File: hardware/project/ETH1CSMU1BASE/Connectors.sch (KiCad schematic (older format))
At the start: 5 parts

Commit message: Schematic developement, new footprints.
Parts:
- J504: renamed from J?; footprint (none) -> ETH1CSMU1:Socket_DIN41612-CaseC1-AC-Male-64Pin-2rows
- gave numbers to parts that had none: 4
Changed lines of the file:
@@
 $Descr A4 11693 8268
 encoding utf-8
-Sheet 5 6
+Sheet 5 7
 Title ""
 Date ""
@@
 $EndDescr
 $Comp
-L Connector:C64AC J?
+L Connector:C64AC J504
 U 1 1 5DE8758D
 P 5550 4150
-F 0 "J?" H 5730 4246 50  0000 L CNN
+F 0 "J504" H 5730 4246 50  0000 L CNN
 F 1 "C64AC" H 5730 4155 50  0000 L CNN
-F 2 "" H 5550 4200 50  0001 C CNN
+F 2 "ETH1CSMU1:Socket_DIN41612-CaseC1-AC-Male-64Pin-2rows" H 5550 4200 50  0001 C CNN
 F 3 " ~" H 5550 4200 50  0001 C CNN
 	1    5550 4150
@@
 	5200 7150 5200 7100
 $Comp
-L power:+24V #PWR?
+L power:+24V #PWR0116
 U 1 1 5DE97137
 P 5150 7100
-F 0 "#PWR?" H 5150 6950 50  0001 C CNN
+F 0 "#PWR0116" H 5150 6950 50  0001 C CNN
 F 1 "+24V" V 5165 7228 50  0000 L CNN
 F 2 "" H 5150 7100 50  0001 C CNN
@@
 	5200 6350 5200 6300
 $Comp
-L power:GND #PWR?
+L power:GND #PWR0117
 U 1 1 5DE992F4
 P 5150 6300
-F 0 "#PWR?" H 5150 6050 50  0001 C CNN
+F 0 "#PWR0117" H 5150 6050 50  0001 C CNN
 F 1 "GND" V 5155 6172 50  0000 R CNN
 F 2 "" H 5150 6300 50  0001 C CNN
@@
 F
 $Comp
-L Connector_Generic:Conn_01x06 J?
+L Connector_Generic:Conn_01x06 J501
 U 1 1 5DEBCC80
 P 2750 2400
-F 0 "J?" H 2668 2817 50  0000 C CNN
+F 0 "J501" H 2668 2817 50  0000 C CNN
 F 1 "Conn_01x06" H 2668 2726 50  0000 C CNN
 F 2 "" H 2750 2400 50  0001 C CNN
@@
 	5200 5250 5250 5250
 $Comp
-L power:Earth #PWR?
+L power:Earth #PWR0118
 U 1 1 5DECE77F
 P 5150 5200
-F 0 "#PWR?" H 5150 4950 50  0001 C CNN
+F 0 "#PWR0118" H 5150 4950 50  0001 C CNN
 F 1 "Earth" H 5150 5050 50  0001 C CNN
 F 2 "" H 5150 5200 50  0001 C CNN
@@
 	5200 4450 5250 4450
 $Comp
-L power:Earth #PWR?
+L power:Earth #PWR0119
 U 1 1 5DED2C4C
 P 5150 4400
-F 0 "#PWR?" H 5150 4150 50  0001 C CNN
+F 0 "#PWR0119" H 5150 4150 50  0001 C CNN
 F 1 "Earth" H 5150 4250 50  0001 C CNN
 F 2 "" H 5150 4400 50  0001 C CNN
@@
 TX-
 $Comp
-L ETH1CSMU1:GND_TRIG #PWR?
+L ETH1CSMU1:GND_TRIG #PWR0120
 U 1 1 5EC065BC
 P 5200 4050
-F 0 "#PWR?" H 5200 3800 50  0001 C CNN
+F 0 "#PWR0120" H 5200 3800 50  0001 C CNN
 F 1 "GND_TRIG" V 5205 3922 50  0000 R CNN
 F 2 "" H 5200 4050 50  0001 C CNN
@@
 	5200 3950 5250 3950
 $Comp
-L ETH1CSMU1:ADuM3151 U?
+L ETH1CSMU1:ADuM3151 U501
 U 1 1 5DCFA591
 P 8050 1800
-F 0 "U?" H 8050 2665 50  0000 C CNN
+F 0 "U501" H 8050 2665 50  0000 C CNN
 F 1 "ADuM3151" H 8050 2574 50  0000 C CNN
 F 2 "" H 9950 2250 50  0001 C CNN
@@
 BASE_~MSS
 $Comp
-L power:+3.3V #PWR?
+L power:+3.3V #PWR0121
 U 1 1 5DCFA59E
 P 7250 1100
-F 0 "#PWR?" H 7250 950 50  0001 C CNN
+F 0 "#PWR0121" H 7250 950 50  0001 C CNN
 F 1 "+3.3V" H 7265 1273 50  0000 C CNN
 F 2 "" H 7250 1100 50  0001 C CNN
@@
 	7250 2400 7350 2400
 $Comp
-L power:GND #PWR?
+L power:GND #PWR0122
 U 1 1 5DCFA5A9
 P 7250 2500
-F 0 "#PWR?" H 7250 2250 50  0001 C CNN
+F 0 "#PWR0122" H 7250 2250 50  0001 C CNN
 F 1 "GND" H 7255 2327 50  0000 C CNN
 F 2 "" H 7250 2500 50  0001 C CNN
@@
 Connection ~ 7250 2400
 $Comp
-L power:+3.3VP #PWR?
+L power:+3.3VP #PWR0123
 U 1 1 5DD4087A
 P 8850 1100
-F 0 "#PWR?" H 9000 1050 50  0001 C CNN
+F 0 "#PWR0123" H 9000 1050 50  0001 C CNN
 F 1 "+3.3VP" H 8870 1243 50  0000 C CNN
 F 2 "" H 8850 1100 50  0001 C CNN
@@
 Connection ~ 8850 2400
 $Comp
-L ETH1CSMU1:GNDS #PWR?
+L ETH1CSMU1:GNDS #PWR0124
 U 1 1 5DD73568
 P 8850 2500
-F 0 "#PWR?" H 8850 2250 50  0001 C CNN
+F 0 "#PWR0124" H 8850 2250 50  0001 C CNN
 F 1 "GNDS" H 8855 2327 50  0000 C CNN
 F 2 "" H 8850 2500 50  0001 C CNN
@@
 	7300 1900 7350 1900
 $Comp
-L Connector_Generic:Conn_02x10_Odd_Even J?
+L Connector_Generic:Conn_02x10_Odd_Even J502
 U 1 1 5DD815E6
 P 8000 3600
-F 0 "J?" H 8050 4217 50  0000 C CNN
+F 0 "J502" H 8050 4217 50  0000 C CNN
 F 1 "Conn_02x10_Odd_Even" H 8050 4126 50  0000 C CNN
 F 2 "" H 8000 3600 50  0001 C CNN
@@
 MODULE_~MSS
 $Comp
-L ETH1CSMU1:GNDS #PWR?
+L ETH1CSMU1:GNDS #PWR0125
 U 1 1 5DE4A93E
 P 7700 4100
-F 0 "#PWR?" H 7700 3850 50  0001 C CNN
+F 0 "#PWR0125" H 7700 3850 50  0001 C CNN
 F 1 "GNDS" V 7705 3972 50  0000 R CNN
 F 2 "" H 7700 4100 50  0001 C CNN
@@
 	7000 3500 7800 3500
 $Comp
-L power:+3.3VP #PWR?
+L power:+3.3VP #PWR0126
 U 1 1 5DE5F329
 P 7750 3200
-F 0 "#PWR?" H 7900 3150 50  0001 C CNN
+F 0 "#PWR0126" H 7900 3150 50  0001 C CNN
 F 1 "+3.3VP" V 7750 3300 50  0000 L CNN
 F 2 "" H 7750 3200 50  0001 C CNN
@@
 	8300 3300 9100 3300
 $Comp
-L power:+3.3VP #PWR?
+L power:+3.3VP #PWR0127
 U 1 1 5DE90B41
 P 8350 3200
-F 0 "#PWR?" H 8500 3150 50  0001 C CNN
+F 0 "#PWR0127" H 8500 3150 50  0001 C CNN
 F 1 "+3.3VP" V 8350 3300 50  0000 L CNN
 F 2 "" H 8350 3200 50  0001 C CNN
@@
 	7750 4100 7800 4100
 $Comp
-L ETH1CSMU1:GNDS #PWR?
+L ETH1CSMU1:GNDS #PWR0128
 U 1 1 5DEB2514
 P 8400 4100
-F 0 "#PWR?" H 8400 3850 50  0001 C CNN
+F 0 "#PWR0128" H 8400 3850 50  0001 C CNN
 F 1 "GNDS" V 8405 3972 50  0000 R CNN
 F 2 "" H 8400 4100 50  0001 C CNN
@@
 	8350 4100 8300 4100
 $Comp
-L ETH1CSMU1:+HV #PWR?
+L ETH1CSMU1:+HV #PWR0129
 U 1 1 5DECC2A8
 P 2400 3500
-F 0 "#PWR?" H 2400 3350 50  0001 C CNN
+F 0 "#PWR0129" H 2400 3350 50  0001 C CNN
 F 1 "+HV" V 2400 3650 50  0000 L CNN
 F 2 "" H 2400 3500 50  0001 C CNN
@@
 	2400 3500 2500 3500
 $Comp
-L ETH1CSMU1:+HV #PWR?
+L ETH1CSMU1:+HV #PWR0130
 U 1 1 5DED1199
 P 3100 3500
-F 0 "#PWR?" H 3100 3350 50  0001 C CNN
+F 0 "#PWR0130" H 3100 3350 50  0001 C CNN
 F 1 "+HV" V 3100 3650 50  0000 L CNN
 F 2 "" H 3100 3500 50  0001 C CNN
@@
 NoConn ~ 3000 3600
 $Comp
-L ETH1CSMU1:-HV #PWR?
+L ETH1CSMU1:-HV #PWR0131
 U 1 1 5DEDEAA7
 P 2400 3700
-F 0 "#PWR?" H 2400 3550 50  0001 C CNN
+F 0 "#PWR0131" H 2400 3550 50  0001 C CNN
 F 1 "-HV" V 2400 3850 50  0000 L CNN
 F 2 "" H 2400 3700 50  0001 C CNN
@@
 	2400 3700 2500 3700
 $Comp
-L ETH1CSMU1:-HV #PWR?
+L ETH1CSMU1:-HV #PWR0132
 U 1 1 5DEE33FC
 P 3100 3700
-F 0 "#PWR?" H 3100 3550 50  0001 C CNN
+F 0 "#PWR0132" H 3100 3550 50  0001 C CNN
 F 1 "-HV" V 3100 3850 50  0000 L CNN
 F 2 "" H 3100 3700 50  0001 C CNN
@@
 	3100 3700 3000 3700
 $Comp
-L ETH1CSMU1:GNDHV #PWR?
+L ETH1CSMU1:GNDHV #PWR0133
 U 1 1 5DF1922C
 P 2400 3950
-F 0 "#PWR?" H 2400 3700 50  0001 C CNN
+F 0 "#PWR0133" H 2400 3700 50  0001 C CNN
 F 1 "GNDHV" V 2405 3822 50  0000 R CNN
 F 2 "" H 2400 3950 50  0001 C CNN
@@
 	2450 3950 2450 4000
 $Comp
-L ETH1CSMU1:GNDHV #PWR?
+L ETH1CSMU1:GNDHV #PWR0134
 U 1 1 5DF55BC0
 P 3100 3950
-F 0 "#PWR?" H 3100 3700 50  0001 C CNN
+F 0 "#PWR0134" H 3100 3700 50  0001 C CNN
 F 1 "GNDHV" V 3105 3822 50  0000 R CNN
 F 2 "" H 3100 3950 50  0001 C CNN
@@
 NoConn ~ 3000 4100
 $Comp
-L power:+5VL #PWR?
+L power:+5VL #PWR0135
 U 1 1 5DF6C00E
 P 2400 4400
-F 0 "#PWR?" H 2400 4250 50  0001 C CNN
+F 0 "#PWR0135" H 2400 4250 50  0001 C CNN
 F 1 "+5VL" V 2415 4527 50  0000 L CNN
 F 2 "" H 2400 4400 50  0001 C CNN
@@
 	2400 4400 2500 4400
 $Comp
-L power:+5VL #PWR?
+L power:+5VL #PWR0136
 U 1 1 5DF71C9F
 P 3100 4400
-F 0 "#PWR?" H 3100 4250 50  0001 C CNN
+F 0 "#PWR0136" H 3100 4250 50  0001 C CNN
 F 1 "+5VL" V 3115 4528 50  0000 L CNN
 F 2 "" H 3100 4400 50  0001 C CNN
@@
 	3100 4400 3000 4400
 $Comp
-L power:+3.3VP #PWR?
+L power:+3.3VP #PWR0137
 U 1 1 5DF78ED7
 P 2400 4500
-F 0 "#PWR?" H 2550 4450 50  0001 C CNN
+F 0 "#PWR0137" H 2550 4450 50  0001 C CNN
 F 1 "+3.3VP" V 2400 4600 50  0000 L CNN
 F 2 "" H 2400 4500 50  0001 C CNN
@@
 	2400 4500 2500 4500
 $Comp
-L power:+3.3VP #PWR?
+L power:+3.3VP #PWR0138
 U 1 1 5DF7F2B1
 P 3100 4500
-F 0 "#PWR?" H 3250 4450 50  0001 C CNN
+F 0 "#PWR0138" H 3250 4450 50  0001 C CNN
 F 1 "+3.3VP" V 3100 4600 50  0000 L CNN
 F 2 "" H 3100 4500 50  0001 C CNN
@@
 	3100 4500 3000 4500
 $Comp
-L power:+15V #PWR?
+L power:+15V #PWR0139
 U 1 1 5DF9592E
 P 2400 4200
-F 0 "#PWR?" H 2400 4050 50  0001 C CNN
+F 0 "#PWR0139" H 2400 4050 50  0001 C CNN
 F 1 "+15V" V 2400 4350 50  0000 L CNN
 F 2 "" H 2400 4200 50  0001 C CNN
@@
 	2400 4200 2500 4200
 $Comp
-L power:+15V #PWR?
+L power:+15V #PWR0140
 U 1 1 5DF9D7C3
 P 3100 4200
-F 0 "#PWR?" H 3100 4050 50  0001 C CNN
+F 0 "#PWR0140" H 3100 4050 50  0001 C CNN
 F 1 "+15V" V 3100 4350 50  0000 L CNN
 F 2 "" H 3100 4200 50  0001 C CNN
@@
 	3100 4200 3000 4200
 $Comp
-L power:-15V #PWR?
+L power:-15V #PWR0141
 U 1 1 5DFBFA3C
 P 2400 4300
-F 0 "#PWR?" H 2400 4400 50  0001 C CNN
+F 0 "#PWR0141" H 2400 4400 50  0001 C CNN
 F 1 "-15V" V 2400 4450 50  0000 L CNN
 F 2 "" H 2400 4300 50  0001 C CNN
@@
 	2400 4300 2500 4300
 $Comp
-L power:-15V #PWR?
+L power:-15V #PWR0142
 U 1 1 5DFCED5E
 P 3100 4300
-F 0 "#PWR?" H 3100 4400 50  0001 C CNN
+F 0 "#PWR0142" H 3100 4400 50  0001 C CNN
 F 1 "-15V" V 3100 4450 50  0000 L CNN
 F 2 "" H 3100 4300 50  0001 C CNN
@@
 	3100 4300 3000 4300
 $Comp
-L Connector_Generic:Conn_02x14_Odd_Even J?
+L Connector_Generic:Conn_02x14_Odd_Even J503
 U 1 1 5DFFC045
 P 2700 4100
-F 0 "J?" H 2750 4917 50  0000 C CNN
+F 0 "J503" H 2750 4917 50  0000 C CNN
 F 1 "Conn_02x14_Odd_Even" H 2750 4826 50  0000 C CNN
 F 2 "" H 2700 4100 50  0001 C CNN
@@
 	3050 4800 3000 4800
 $Comp
-L ETH1CSMU1:GNDS #PWR?
+L ETH1CSMU1:GNDS #PWR0143
 U 1 1 5E00D610
 P 2400 4750
-F 0 "#PWR?" H 2400 4500 50  0001 C CNN
+F 0 "#PWR0143" H 2400 4500 50  0001 C CNN
 F 1 "GNDS" V 2400 4600 50  0000 R CNN
 F 2 "" H 2400 4750 50  0001 C CNN
@@
 	2450 4750 2450 4800
 $Comp
-L ETH1CSMU1:GNDS #PWR?
+L ETH1CSMU1:GNDS #PWR0144
 U 1 1 5E015B37
 P 3100 4750
-F 0 "#PWR?" H 3100 4500 50  0001 C CNN
+F 0 "#PWR0144" H 3100 4500 50  0001 C CNN
 F 1 "GNDS" V 3100 4600 50  0000 R CNN
 F 2 "" H 3100 4750 50  0001 C CNN

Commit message: Schematic design.
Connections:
- net labels removed: +15V, +5VL, +HV, -15V, -HV, GNDHV
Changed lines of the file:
@@
 $Descr A4 11693 8268
 encoding utf-8
-Sheet 5 7
+Sheet 5 9
 Title ""
 Date ""
@@
 Wire Wire Line
 	8350 4100 8300 4100
-$Comp
-L ETH1CSMU1:+HV #PWR0129
-U 1 1 5DECC2A8
-P 2400 3500
-F 0 "#PWR0129" H 2400 3350 50  0001 C CNN
-F 1 "+HV" V 2400 3650 50  0000 L CNN
-F 2 "" H 2400 3500 50  0001 C CNN
-F 3 "" H 2400 3500 50  0001 C CNN
-	1    2400 3500
-	0    -1   -1   0
-$EndComp
 Wire Wire Line
 	2400 3500 2500 3500
-$Comp
-L ETH1CSMU1:+HV #PWR0130
-U 1 1 5DED1199
-P 3100 3500
-F 0 "#PWR0130" H 3100 3350 50  0001 C CNN
-F 1 "+HV" V 3100 3650 50  0000 L CNN
-F 2 "" H 3100 3500 50  0001 C CNN
-F 3 "" H 3100 3500 50  0001 C CNN
-	1    3100 3500
-	0    1    1    0
-$EndComp
 Wire Wire Line
 	3100 3500 3000 3500
 NoConn ~ 2500 3600
 NoConn ~ 3000 3600
-$Comp
-L ETH1CSMU1:-HV #PWR0131
-U 1 1 5DEDEAA7
-P 2400 3700
-F 0 "#PWR0131" H 2400 3550 50  0001 C CNN
-F 1 "-HV" V 2400 3850 50  0000 L CNN
-F 2 "" H 2400 3700 50  0001 C CNN
-F 3 "" H 2400 3700 50  0001 C CNN
-	1    2400 3700
-	0    -1   -1   0
-$EndComp
 Wire Wire Line
 	2400 3700 2500 3700
-$Comp
-L ETH1CSMU1:-HV #PWR0132
-U 1 1 5DEE33FC
-P 3100 3700
-F 0 "#PWR0132" H 3100 3550 50  0001 C CNN
-F 1 "-HV" V 3100 3850 50  0000 L CNN
-F 2 "" H 3100 3700 50  0001 C CNN
-F 3 "" H 3100 3700 50  0001 C CNN
-	1    3100 3700
-	0    1    1    0
-$EndComp
 Wire Wire Line
 	3100 3700 3000 3700
-$Comp
-L ETH1CSMU1:GNDHV #PWR0133
-U 1 1 5DF1922C
-P 2400 3950
-F 0 "#PWR0133" H 2400 3700 50  0001 C CNN
-F 1 "GNDHV" V 2405 3822 50  0000 R CNN
-F 2 "" H 2400 3950 50  0001 C CNN
-F 3 "" H 2400 3950 50  0001 C CNN
-	1    2400 3950
-	0    1    1    0
-$EndComp
 NoConn ~ 2500 3800
 NoConn ~ 3000 3800
@@
 Wire Wire Line
 	2450 3950 2450 4000
-$Comp
-L ETH1CSMU1:GNDHV #PWR0134
-U 1 1 5DF55BC0
-P 3100 3950
-F 0 "#PWR0134" H 3100 3700 50  0001 C CNN
-F 1 "GNDHV" V 3105 3822 50  0000 R CNN
-F 2 "" H 3100 3950 50  0001 C CNN
-F 3 "" H 3100 3950 50  0001 C CNN
-	1    3100 3950
-	0    -1   -1   0
-$EndComp
 Wire Wire Line
 	3000 4000 3050 4000
@@
 NoConn ~ 2500 4100
 NoConn ~ 3000 4100
-$Comp
-L power:+5VL #PWR0135
-U 1 1 5DF6C00E
-P 2400 4400
-F 0 "#PWR0135" H 2400 4250 50  0001 C CNN
-F 1 "+5VL" V 2415 4527 50  0000 L CNN
-F 2 "" H 2400 4400 50  0001 C CNN
-F 3 "" H 2400 4400 50  0001 C CNN
-	1    2400 4400
-	0    -1   -1   0
-$EndComp
 Wire Wire Line
 	2400 4400 2500 4400
-$Comp
-L power:+5VL #PWR0136
-U 1 1 5DF71C9F
-P 3100 4400
-F 0 "#PWR0136" H 3100 4250 50  0001 C CNN
-F 1 "+5VL" V 3115 4528 50  0000 L CNN
-F 2 "" H 3100 4400 50  0001 C CNN
-F 3 "" H 3100 4400 50  0001 C CNN
-	1    3100 4400
-	0    1    1    0
-$EndComp
 Wire Wire Line
 	3100 4400 3000 4400
-$Comp
-L power:+3.3VP #PWR0137
-U 1 1 5DF78ED7
-P 2400 4500
-F 0 "#PWR0137" H 2550 4450 50  0001 C CNN
-F 1 "+3.3VP" V 2400 4600 50  0000 L CNN
-F 2 "" H 2400 4500 50  0001 C CNN
-F 3 "" H 2400 4500 50  0001 C CNN
-	1    2400 4500
-	0    -1   -1   0
-$EndComp
 Wire Wire Line
 	2400 4500 2500 4500
-$Comp
-L power:+3.3VP #PWR0138
-U 1 1 5DF7F2B1
-P 3100 4500
-F 0 "#PWR0138" H 3250 4450 50  0001 C CNN
-F 1 "+3.3VP" V 3100 4600 50  0000 L CNN
-F 2 "" H 3100 4500 50  0001 C CNN
-F 3 "" H 3100 4500 50  0001 C CNN
-	1    3100 4500
-	0    1    1    0
-$EndComp
 Wire Wire Line
 	3100 4500 3000 4500
-$Comp
-L power:+15V #PWR0139
-U 1 1 5DF9592E
-P 2400 4200
-F 0 "#PWR0139" H 2400 4050 50  0001 C CNN
-F 1 "+15V" V 2400 4350 50  0000 L CNN
-F 2 "" H 2400 4200 50  0001 C CNN
-F 3 "" H 2400 4200 50  0001 C CNN
-	1    2400 4200
-	0    -1   -1   0
-$EndComp
 Wire Wire Line
 	2400 4200 2500 4200
-$Comp
-L power:+15V #PWR0140
-U 1 1 5DF9D7C3
-P 3100 4200
-F 0 "#PWR0140" H 3100 4050 50  0001 C CNN
-F 1 "+15V" V 3100 4350 50  0000 L CNN
-F 2 "" H 3100 4200 50  0001 C CNN
-F 3 "" H 3100 4200 50  0001 C CNN
-	1    3100 4200
-	0    1    1    0
-$EndComp
 Wire Wire Line
 	3100 4200 3000 4200
-$Comp
-L power:-15V #PWR0141
-U 1 1 5DFBFA3C
-P 2400 4300
-F 0 "#PWR0141" H 2400 4400 50  0001 C CNN
-F 1 "-15V" V 2400 4450 50  0000 L CNN
-F 2 "" H 2400 4300 50  0001 C CNN
-F 3 "" H 2400 4300 50  0001 C CNN
-	1    2400 4300
-	0    -1   -1   0
-$EndComp
 Wire Wire Line
 	2400 4300 2500 4300
-$Comp
-L power:-15V #PWR0142
-U 1 1 5DFCED5E
-P 3100 4300
-F 0 "#PWR0142" H 3100 4400 50  0001 C CNN
-F 1 "-15V" V 3100 4450 50  0000 L CNN
-F 2 "" H 3100 4300 50  0001 C CNN
-F 3 "" H 3100 4300 50  0001 C CNN
-	1    3100 4300
-	0    1    1    0
-$EndComp
 Wire Wire Line
 	3100 4300 3000 4300
@@
 Wire Wire Line
 	3050 4800 3000 4800
-$Comp
-L ETH1CSMU1:GNDS #PWR0143
-U 1 1 5E00D610
-P 2400 4750
-F 0 "#PWR0143" H 2400 4500 50  0001 C CNN
-F 1 "GNDS" V 2400 4600 50  0000 R CNN
-F 2 "" H 2400 4750 50  0001 C CNN
-F 3 "" H 2400 4750 50  0001 C CNN
-	1    2400 4750
-	0    1    1    0
-$EndComp
 Wire Wire Line
 	2400 4750 2450 4750
@@
 Wire Wire Line
 	2450 4750 2450 4800
-$Comp
-L ETH1CSMU1:GNDS #PWR0144
-U 1 1 5E015B37
-P 3100 4750
-F 0 "#PWR0144" H 3100 4500 50  0001 C CNN
-F 1 "GNDS" V 3100 4600 50  0000 R CNN
-F 2 "" H 3100 4750 50  0001 C CNN
-F 3 "" H 3100 4750 50  0001 C CNN
-	1    3100 4750
-	0    -1   -1   0
-$EndComp
 Wire Wire Line
 	3100 4750 3050 4750

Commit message: Power supply design
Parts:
- removed J502: Conn_02x10_Odd_Even, symbol Connector_Generic:Conn_02x10_Odd_Even
- removed J503: Conn_02x14_Odd_Even, symbol Connector_Generic:Conn_02x14_Odd_Even
- added J?: Conn_02x08_Odd_Even, symbol Connector_Generic:Conn_02x08_Odd_Even
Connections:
- net labels added: +3.3VF, GNDF
- net labels removed: +3.3VP, GNDS
- wire segments 152 -> 112
- no-connect marks 32 -> 26
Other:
- moved on the sheet: J501, U501

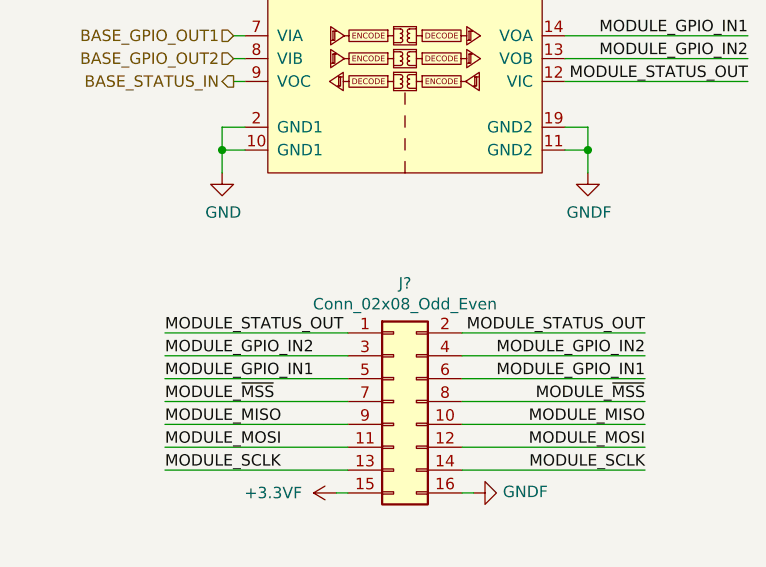
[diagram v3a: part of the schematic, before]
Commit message: Footprint assigment
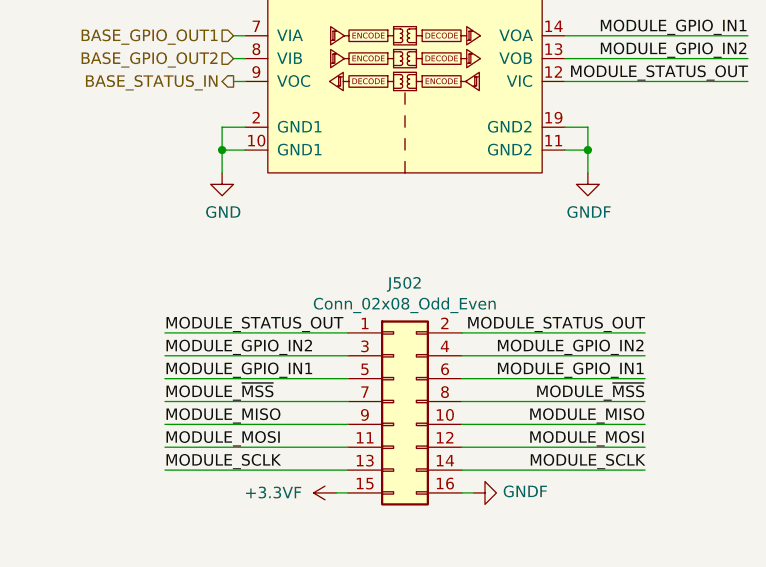
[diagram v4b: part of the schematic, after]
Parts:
- U501: footprint (none) -> Package_SO:SSOP-20_5.3x7.2mm_P0.65mm
- gave numbers to parts that had none: 1
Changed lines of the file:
@@
 F 0 "U501" H 9000 2515 50  0000 C CNN
 F 1 "ADuM3151" H 9000 2424 50  0000 C CNN
-F 2 "" H 10900 2100 50  0001 C CNN
+F 2 "Package_SO:SSOP-20_5.3x7.2mm_P0.65mm" H 10900 2100 50  0001 C CNN
 F 3 "" H 10900 2100 50  0001 C CNN
 	1    9000 1650
@@
 MODULE_GPIO_IN1
 $Comp
-L ETH1CSMU1:+3.3VF #PWR?
+L ETH1CSMU1:+3.3VF #PWR0108
 U 1 1 6828C08F
 P 9800 950
-F 0 "#PWR?" H 9800 800 50  0001 C CNN
+F 0 "#PWR0108" H 9800 800 50  0001 C CNN
 F 1 "+3.3VF" H 9815 1123 50  0000 C CNN
 F 2 "" H 9800 950 50  0001 C CNN
@@
 $EndComp
 $Comp
-L ETH1CSMU1:GNDF #PWR?
+L ETH1CSMU1:GNDF #PWR0123
 U 1 1 6828CBFD
 P 9800 2350
-F 0 "#PWR?" H 9800 2100 50  0001 C CNN
+F 0 "#PWR0123" H 9800 2100 50  0001 C CNN
 F 1 "GNDF" H 9805 2177 50  0000 C CNN
 F 2 "" H 9800 2350 50  0001 C CNN
@@
 $EndComp
 $Comp
-L ETH1CSMU1:+3.3VF #PWR?
+L ETH1CSMU1:+3.3VF #PWR0124
 U 1 1 6829671C
 P 8700 3750
-F 0 "#PWR?" H 8700 3600 50  0001 C CNN
+F 0 "#PWR0124" H 8700 3600 50  0001 C CNN
 F 1 "+3.3VF" V 8700 3900 50  0000 L CNN
 F 2 "" H 8700 3750 50  0001 C CNN
@@
 $EndComp
 $Comp
-L ETH1CSMU1:GNDF #PWR?
+L ETH1CSMU1:GNDF #PWR0125
 U 1 1 682984F3
 P 9300 3750
-F 0 "#PWR?" H 9300 3500 50  0001 C CNN
+F 0 "#PWR0125" H 9300 3500 50  0001 C CNN
 F 1 "GNDF" V 9305 3622 50  0000 R CNN
 F 2 "" H 9300 3750 50  0001 C CNN
@@
 	9300 3750 9250 3750
 $Comp
-L Connector_Generic:Conn_02x08_Odd_Even J?
+L Connector_Generic:Conn_02x08_Odd_Even J502
 U 1 1 682E02F4
 P 8950 3350
-F 0 "J?" H 9000 3867 50  0000 C CNN
+F 0 "J502" H 9000 3867 50  0000 C CNN
 F 1 "Conn_02x08_Odd_Even" H 9000 3776 50  0000 C CNN
 F 2 "" H 8950 3350 50  0001 C CNN

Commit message: Footprint assignment
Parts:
- removed J501: Conn_01x06, symbol Connector_Generic:Conn_01x06
- removed J502: Conn_02x08_Odd_Even, symbol Connector_Generic:Conn_02x08_Odd_Even
- removed U501: ADuM3151, Package_SO:SSOP-20_5.3x7.2mm_P0.65mm, symbol ETH1CSMU1:ADuM3151
- added J301: Conn_01x06_Female, symbol Connector:Conn_01x06_Female
- added J302: Conn_01x04_Female, symbol Connector:Conn_01x04_Female
- renumbered J504 to J402
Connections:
- net A: now also J301.1 (Pin_1)
- net B: now also J301.2 (Pin_2)
- net C: now also J301.3 (Pin_3)
- net D: now also J301.4 (Pin_4)
- net E: now also J301.5 (Pin_5)
- net F: now also J301.6 (Pin_6)
- net RX+: now also J302.1 (Pin_1)
- net RX-: now also J302.2 (Pin_2)
- net TX+: now also J302.3 (Pin_3)
- net TX-: now also J302.4 (Pin_4)
- no-connect marks 26 -> 34
